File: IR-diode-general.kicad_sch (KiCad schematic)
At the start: 0 parts

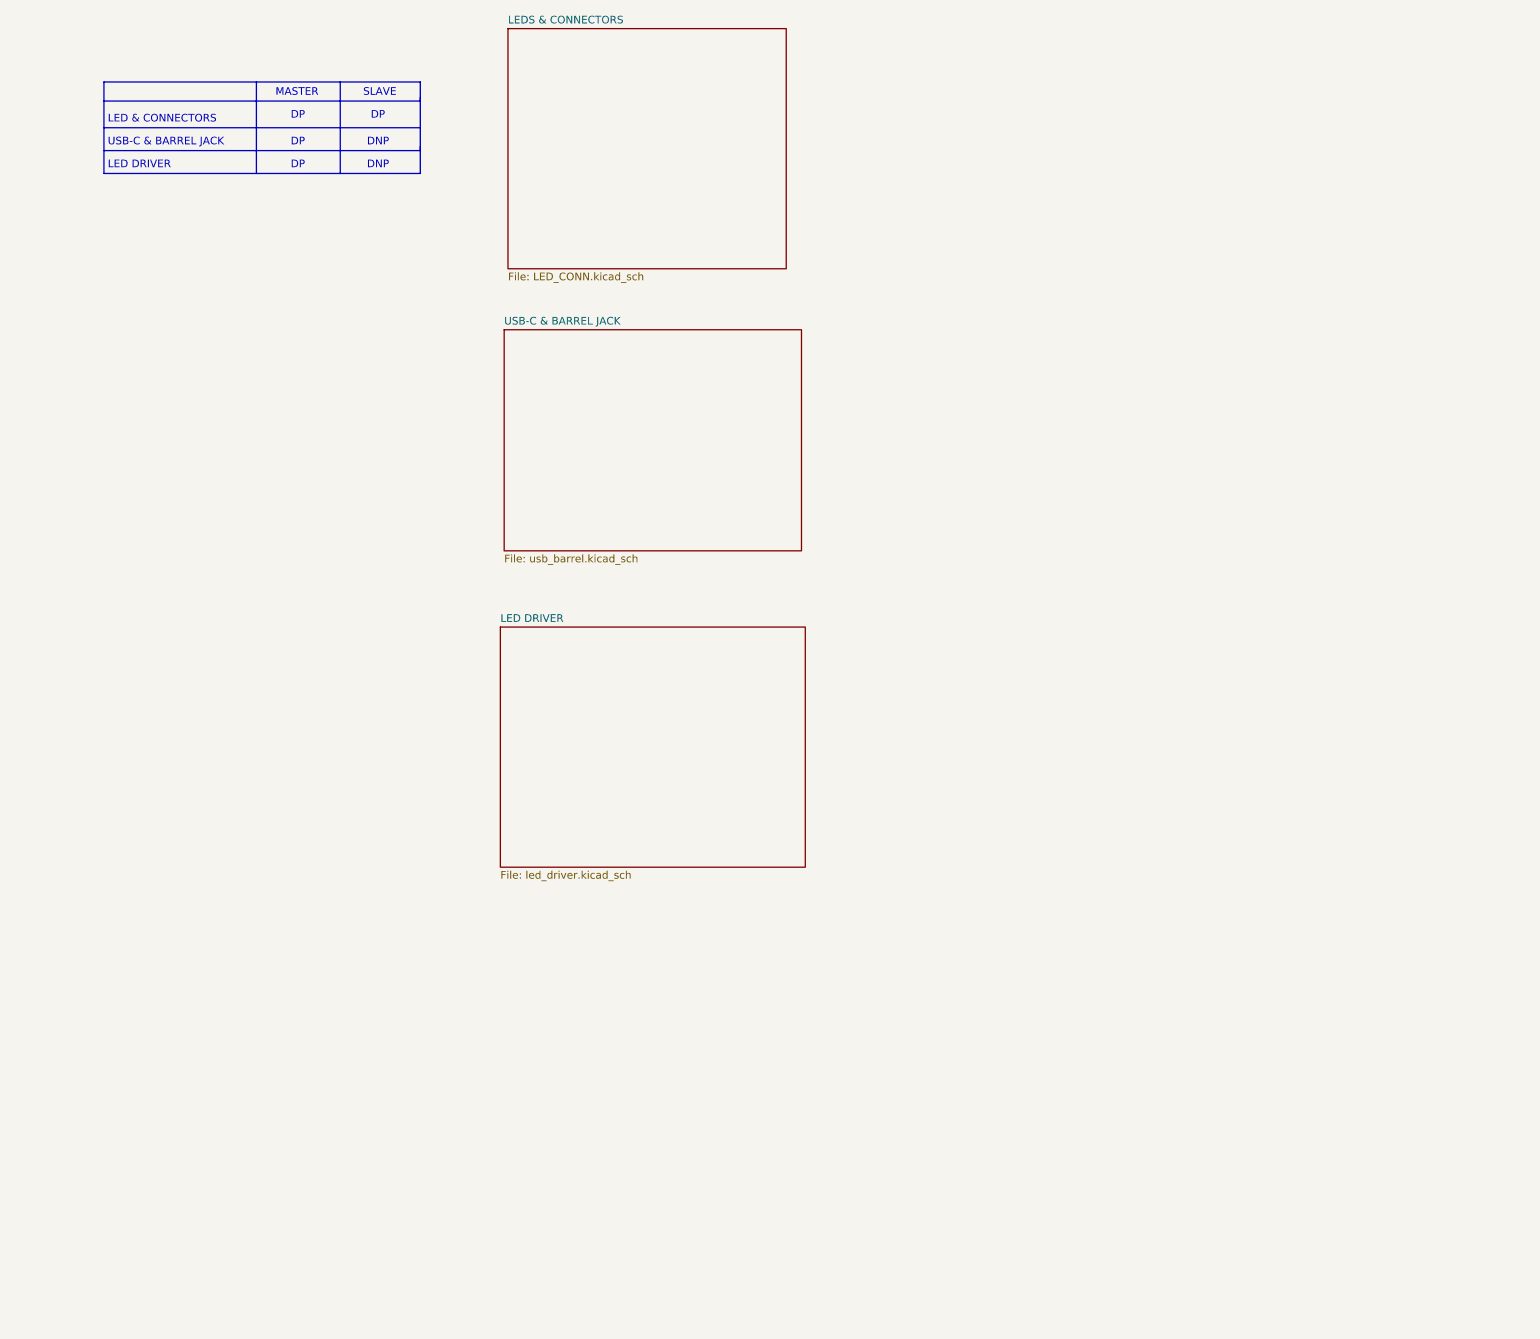
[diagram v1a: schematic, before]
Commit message: Add 100n to VBUS, schematic cleanup
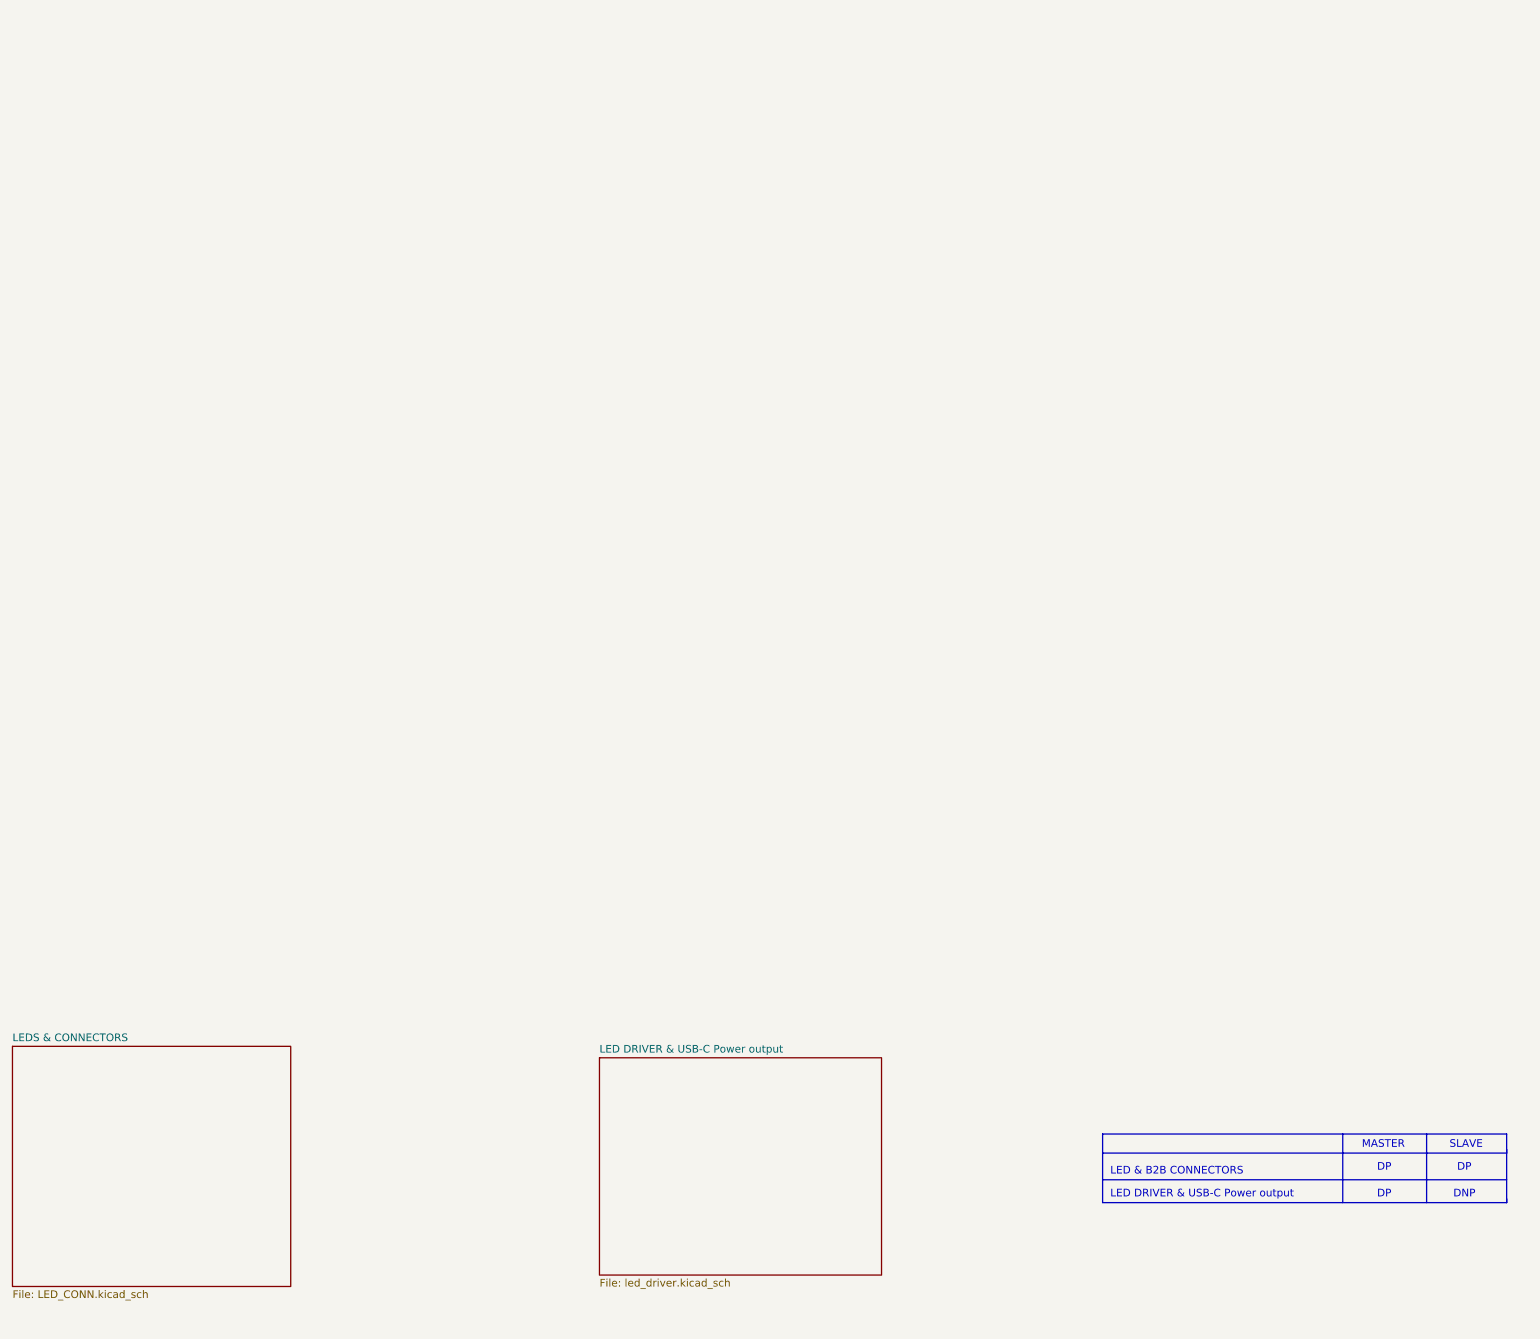
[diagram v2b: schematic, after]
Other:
- sheet LED DRIVER renamed LED DRIVER & USB-C Power output
- removed sheet USB-C & BARREL JACK
- note added: "LED & B2B CONNECTORS"
- note added: "LED DRIVER & USB-C Power output"
- note removed: "LED & CONNECTORS"
- note removed: "LED DRIVER"
- note removed: "USB-C & BARREL JACK"

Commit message: Added signage
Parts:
- added N1: antmicro_logo, antmicro-footprints:antmicro-logo_scaled_12mm, symbol antmicroMechanicalParts:antmicro_logo
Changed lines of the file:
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@@
     (effects (font (size 1.27 1.27)) (justify left bottom))
+  )
+  (symbol (lib_id "antmicroMechanicalParts:antmicro_logo") (at 349.885 236.855 180) (unit 1)
+    (in_bom yes) (on_board yes) (fields_autoplaced)
+    (property "Reference" "N1" (id 0) (at 342.265 241.6875 0)
+      (effects (font (size 1.27 1.27) (thickness 0.15)) (justify left))
+    )
+    (property "Value" "antmicro_logo" (id 1) (at 342.265 239.1475 0)
+      (effects (font (size 1.27 1.27) (thickness 0.15)) (justify left))
+    )
+    (property "Footprint" "antmicro-footprints:antmicro-logo_scaled_12mm" (id 2) (at 334.645 226.695 0)
+      (effects (font (size 1.27 1.27) (thickness 0.15)) (justify left bottom) hide)
+    )
+    (property "Datasheet" "" (id 3) (at 334.645 224.155 0)
+      (effects (font (size 1.27 1.27) (thickness 0.15)) (justify left bottom) hide)
+    )
+    (property "Copyright" "Copyright (c) 2023 Antmicro" (id 4) (at 334.645 221.615 0)
+      (effects (font (size 1.27 1.27) (thickness 0.15)) (justify left bottom) hide)
+    )
+    (property "License" "Apache-2.0 License" (id 5) (at 334.645 219.075 0)
+      (effects (font (size 1.27 1.27) (thickness 0.15)) (justify left bottom) hide)
+    )
+    (property "Manufacturer" "None" (id 6) (at 342.265 236.6075 0)
+      (effects (font (size 1.27 1.27)) (justify left))
+    )
   )
   (sheet (at 131.445 196.215) (size 46.355 40.005) (fields_autoplaced)
@@
       (reference "L2") (unit 1) (value "TFM252012ALMA3R3MTAA") (footprint "antmicro-footprints:L_1008_2520Metric")
     )
+    (path "/e3b00d88-087f-4e06-b63c-4aca4c7bea49"
+      (reference "N1") (unit 1) (value "antmicro_logo") (footprint "antmicro-footprints:antmicro-logo_scaled_12mm")
+    )
     (path "/04f57430-8668-4227-a3f5-414daa4e8985/525b2cf7-1cc0-4346-ad9e-29d535c1d5cc"

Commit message: Configured page properties
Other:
- company: (none) -> Antmicro Ltd.
- title: (none) -> 1050nm IR LED Driver
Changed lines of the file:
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@@
 (kicad_sch (version 20211123) (generator eeschema)
   (paper "A3")
+  (title_block
+    (title "1050nm IR LED Driver")
+    (date "2023-04-14")
+    (rev "1.0.0")
+    (company "Antmicro Ltd.")
+    (comment 1 "www.antmicro.com")
+  )
   (polyline (pts (xy 380.365 222.25) (xy 380.365 221.615))
     (stroke (width 0) (type default) (color 0 0 0 0))

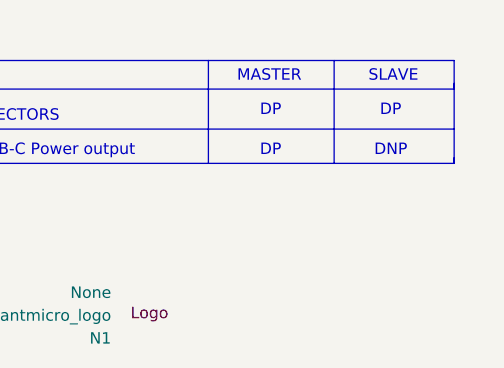
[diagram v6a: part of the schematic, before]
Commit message: Added OSHW marking
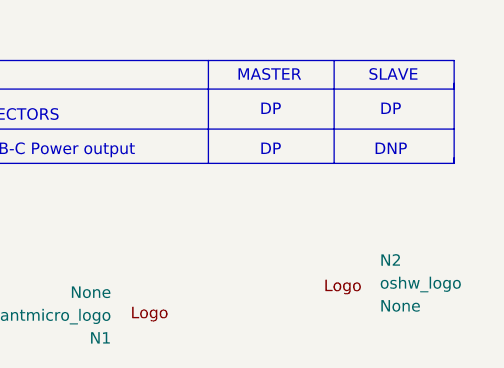
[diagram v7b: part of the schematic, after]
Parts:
- added N2: oshw_logo, antmicro-footprints:oshw-logo, symbol antmicroMechanicalParts:oshw_logo
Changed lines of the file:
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@@
     (effects (font (size 1.27 1.27)) (justify left bottom))
+  )
+  (symbol (lib_id "antmicroMechanicalParts:oshw_logo") (at 365.125 235.585 0) (unit 1)
+    (in_bom yes) (on_board yes) (fields_autoplaced)
+    (property "Reference" "N2" (id 0) (at 372.11 233.0385 0)
+      (effects (font (size 1.27 1.27) (thickness 0.15)) (justify left))
+    )
+    (property "Value" "oshw_logo" (id 1) (at 372.11 235.5785 0)
+      (effects (font (size 1.27 1.27) (thickness 0.15)) (justify left))
+    )
+    (property "Footprint" "antmicro-footprints:oshw-logo" (id 2) (at 380.365 245.745 0)
+      (effects (font (size 1.27 1.27) (thickness 0.15)) (justify left bottom) hide)
+    )
+    (property "Datasheet" "" (id 3) (at 380.365 248.285 0)
+      (effects (font (size 1.27 1.27) (thickness 0.15)) (justify left bottom) hide)
+    )
+    (property "Copyright" "Copyright (c) 2023 Antmicro" (id 4) (at 380.365 250.825 0)
+      (effects (font (size 1.27 1.27) (thickness 0.15)) (justify left bottom) hide)
+    )
+    (property "License" "Apache-2.0 License" (id 5) (at 380.365 253.365 0)
+      (effects (font (size 1.27 1.27) (thickness 0.15)) (justify left bottom) hide)
+    )
+    (property "Manufacturer" "None" (id 6) (at 372.11 238.1185 0)
+      (effects (font (size 1.27 1.27)) (justify left))
+    )
   )
   (symbol (lib_id "antmicroMechanicalParts:antmicro_logo") (at 349.885 236.855 180) (unit 1)
@@
       (reference "N1") (unit 1) (value "antmicro_logo") (footprint "antmicro-footprints:antmicro-logo_scaled_12mm")
     )
+    (path "/1b0c8774-ceb9-4874-83b5-1cbac8231cfd"
+      (reference "N2") (unit 1) (value "oshw_logo") (footprint "antmicro-footprints:oshw-logo")
+    )
     (path "/04f57430-8668-4227-a3f5-414daa4e8985/525b2cf7-1cc0-4346-ad9e-29d535c1d5cc"
